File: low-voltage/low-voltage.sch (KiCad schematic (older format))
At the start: 40 parts, among them J1 Conn_Coaxial, J2 Conn_01x01, J3 Conn_01x01, J4 Conn_01x01, J5 Conn_01x01, J6 Conn_01x01, J7 Conn_01x01, J8 Conn_01x01, Q1 2N4401, SW1 SW_SPST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

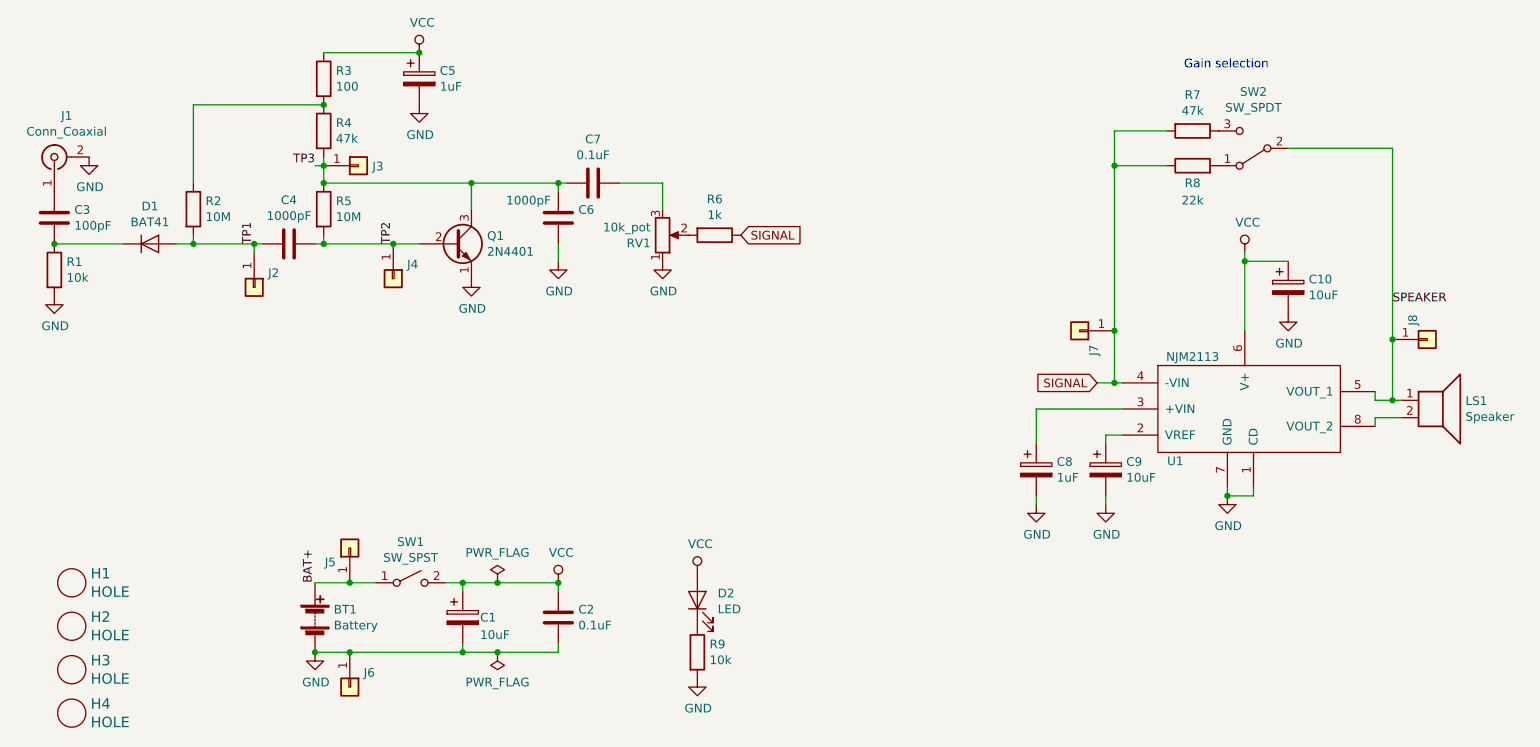
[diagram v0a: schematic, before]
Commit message: Change low voltage to use lm386 instead of njm2113
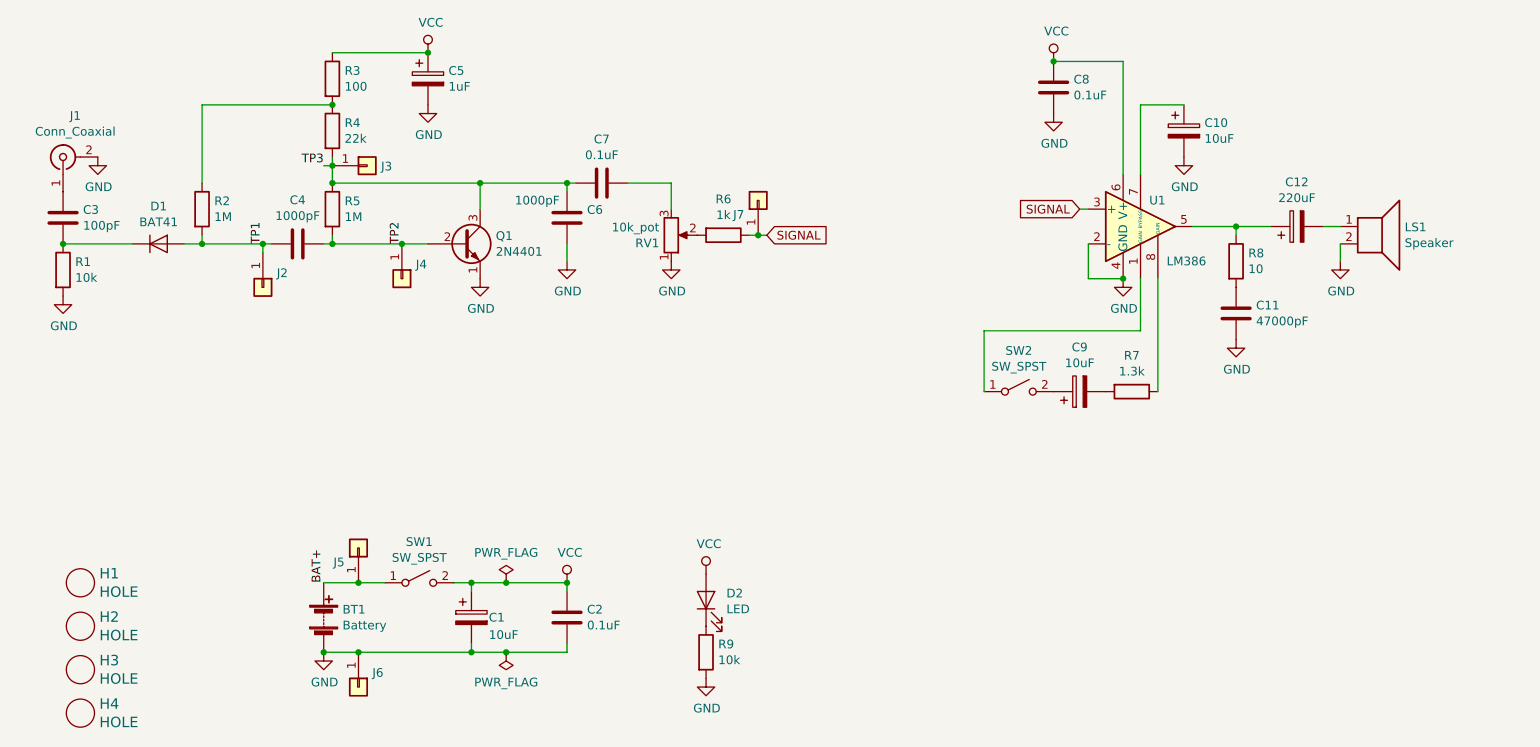
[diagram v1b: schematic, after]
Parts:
- removed C8: 1uF, Capacitor_THT:CP_Radial_D5.0mm_P2.00mm, symbol Device:CP
- removed J8: Conn_01x01, Connector_PinHeader_2.54mm:PinHeader_1x01_P2.54mm_Vertical, symbol Connector_Generic:Conn_01x01
- removed SW2: SW_SPDT, homebrew:‎EG1206‎_SLIDE_SWITCH, symbol Switch:SW_SPDT
- removed U1: NJM2113, Package_DIP:DIP-8_W7.62mm, symbol Homebrew:NJM2113
- added C11: 47000pF, Capacitor_THT:C_Disc_D3.8mm_W2.6mm_P2.50mm, symbol Device:C
- added C12: 220uF, Capacitor_THT:CP_Radial_D6.3mm_P2.50mm, symbol Device:CP
- added C8: 0.1uF, Capacitor_THT:C_Disc_D5.1mm_W3.2mm_P5.00mm, symbol Device:C
- added SW2: SW_SPST, homebrew:‎EG1206‎_SLIDE_SWITCH, symbol Switch:SW_SPST
- added U1: LM386, Package_DIP:DIP-8_W7.62mm, symbol Amplifier_Audio:LM386
- R2, R5: value 10M -> 1M
- R4: value 47k -> 22k
- R7: value 47k -> 1.3k
- R8: value 22k -> 10
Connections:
- net GND: now also LS1.2, C11.2, C8.2, U1.2 (-), U1.4 (GND); no longer C9.2
- net SIGNAL: now also U1.3 (+); no longer R7.2, R8.1
- net VCC: now also C8.1, U1.6 (V+); no longer C10.1
- net at C9.1: now also SW2.2 (B)
- net at R7.1: now also U1.8 (GAIN)
- net at R8.2: now also C11.1
- net SPEAKER: no longer names the net of LS1.1
- net SPEAKER: now also C12.2
- new net: SW2.1 (A), U1.1 (GAIN)
- new net: C12.1, R8.1, U1.5
- new net: C10.1, U1.7 (BYPASS)
- new net: C9.2, R7.2
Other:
- note removed: "Gain selection"
- moved on the sheet: BT1, C1, C2, C3, C4, C5, C6, C7, D1, D2, H1, H2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

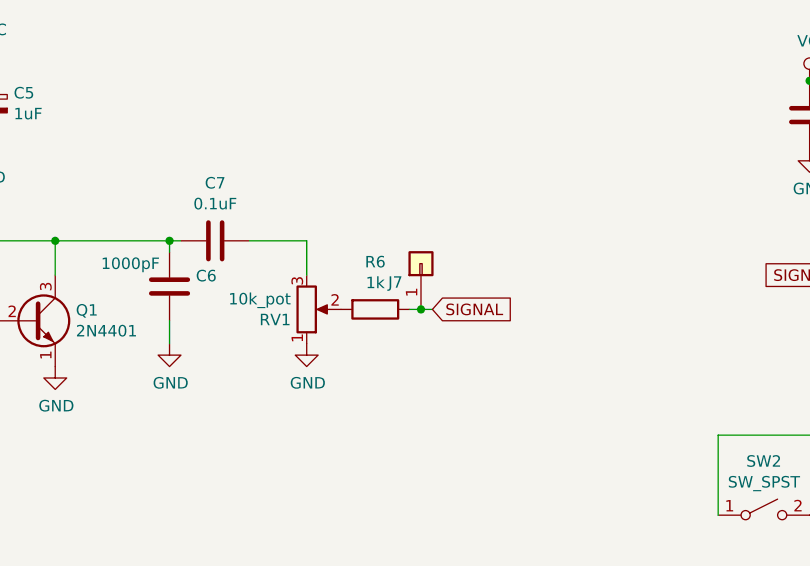
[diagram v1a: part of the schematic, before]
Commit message: Place components for low voltage
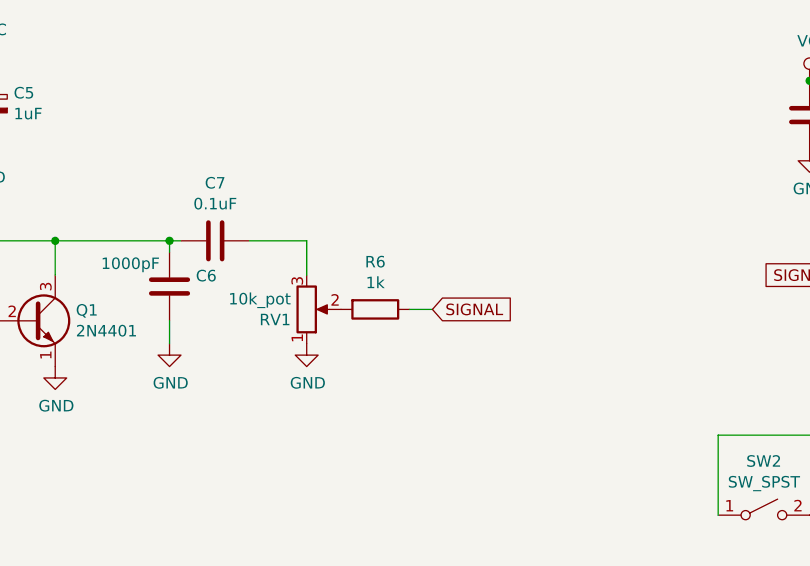
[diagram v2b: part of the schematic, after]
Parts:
- removed J7: Conn_01x01, Connector_PinHeader_2.54mm:PinHeader_1x01_P2.54mm_Vertical, symbol Connector_Generic:Conn_01x01
- BT1: footprint Battery:BatteryHolder_Keystone_2479_3xAAA -> homebrew:BatteryHolder_Keystone_2481_4xAAA

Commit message: Final design for low voltage (v2.0)
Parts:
- added C13: 220uF, Capacitor_THT:CP_Radial_D6.3mm_P2.50mm, symbol Device:CP
- J5, J6: footprint Connector_PinHeader_2.54mm:PinHeader_1x01_P2.54mm_Vertical -> homebrew:ALLIGATOR_CLIP_SLOT
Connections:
- net BAT+: no longer J5.1 (Pin_1)
- net GND: now also C13.2
- net VCC: now also J5.1 (Pin_1), C13.1
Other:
- moved on the sheet: D2, J5, R9
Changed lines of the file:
@@
 	1    0    0    -1
 $EndComp
-Wire Wire Line
-	2250 3800 2450 3800
 $Comp
 L power:VCC #PWR02
 U 1 1 5E8DFA2E
-P 3650 3800
-F 0 "#PWR02" H 3650 3650 50  0001 C CNN
-F 1 "VCC" H 3667 3973 50  0000 C CNN
-F 2 "" H 3650 3800 50  0001 C CNN
-F 3 "" H 3650 3800 50  0001 C CNN
-	1    3650 3800
+P 4200 3800
+F 0 "#PWR02" H 4200 3650 50  0001 C CNN
+F 1 "VCC" H 4217 3973 50  0000 C CNN
+F 2 "" H 4200 3800 50  0001 C CNN
+F 3 "" H 4200 3800 50  0001 C CNN
+	1    4200 3800
 	1    0    0    -1
 $EndComp
@@
 L Connector_Generic:Conn_01x01 J?
 U 1 1 5E9E11D0
-P 2450 3600
+P 3900 3600
 AR Path="/5E7D3582/5E9E11D0" Ref="J?"  Part="1"
 AR Path="/5E9E11D0" Ref="J5"  Part="1"
-F 0 "J5" V 2368 3680 50  0000 L CNN
-F 1 "Conn_01x01" V 2413 3680 50  0001 L CNN
-F 2 "Connector_PinHeader_2.54mm:PinHeader_1x01_P2.54mm_Vertical" H 2450 3600 50  0001 C CNN
-F 3 "~" H 2450 3600 50  0001 C CNN
-	1    2450 3600
+F 0 "J5" V 3818 3680 50  0000 L CNN
+F 1 "Conn_01x01" V 3863 3680 50  0001 L CNN
+F 2 "homebrew:ALLIGATOR_CLIP_SLOT" H 3900 3600 50  0001 C CNN
+F 3 "~" H 3900 3600 50  0001 C CNN
+	1    3900 3600
 	0    -1   -1   0
 $EndComp
-Connection ~ 2450 3800
-Wire Wire Line
-	2450 3800 2600 3800
 $Comp
 L Connector_Generic:Conn_01x01 J?
@@
 F 0 "J6" V 2368 4480 50  0000 L CNN
 F 1 "Conn_01x01" V 2413 4480 50  0001 L CNN
-F 2 "Connector_PinHeader_2.54mm:PinHeader_1x01_P2.54mm_Vertical" H 2450 4400 50  0001 C CNN
+F 2 "homebrew:ALLIGATOR_CLIP_SLOT" H 2450 4400 50  0001 C CNN
 F 3 "~" H 2450 4400 50  0001 C CNN
 	1    2450 4400
@@
 L Device:LED D2
 U 1 1 5EA05149
-P 4450 3900
-F 0 "D2" V 4489 3783 50  0000 R CNN
-F 1 "LED" V 4398 3783 50  0000 R CNN
-F 2 "LED_THT:LED_D5.0mm_Horizontal_O1.27mm_Z9.0mm" H 4450 3900 50  0001 C CNN
-F 3 "~" H 4450 3900 50  0001 C CNN
-	1    4450 3900
+P 5350 3900
+F 0 "D2" V 5389 3783 50  0000 R CNN
+F 1 "LED" V 5298 3783 50  0000 R CNN
+F 2 "LED_THT:LED_D5.0mm_Horizontal_O1.27mm_Z9.0mm" H 5350 3900 50  0001 C CNN
+F 3 "~" H 5350 3900 50  0001 C CNN
+	1    5350 3900
 	0    -1   -1   0
 $EndComp
@@
 L Device:R R?
 U 1 1 5EA0679F
-P 4450 4200
+P 5350 4200
 AR Path="/5E7D3582/5EA0679F" Ref="R?"  Part="1"
 AR Path="/5EA0679F" Ref="R9"  Part="1"
-F 0 "R9" H 4520 4246 50  0000 L CNN
-F 1 "10k" H 4520 4155 50  0000 L CNN
-F 2 "Resistor_THT:R_Axial_DIN0207_L6.3mm_D2.5mm_P10.16mm_Horizontal" V 4380 4200 50  0001 C CNN
-F 3 "~" H 4450 4200 50  0001 C CNN
-	1    4450 4200
+F 0 "R9" H 5420 4246 50  0000 L CNN
+F 1 "10k" H 5420 4155 50  0000 L CNN
+F 2 "Resistor_THT:R_Axial_DIN0207_L6.3mm_D2.5mm_P10.16mm_Horizontal" V 5280 4200 50  0001 C CNN
+F 3 "~" H 5350 4200 50  0001 C CNN
+	1    5350 4200
 	1    0    0    -1
 $EndComp
@@
 L power:GND #PWR011
 U 1 1 5EA06DDD
-P 4450 4350
-F 0 "#PWR011" H 4450 4100 50  0001 C CNN
-F 1 "GND" H 4455 4177 50  0000 C CNN
-F 2 "" H 4450 4350 50  0001 C CNN
-F 3 "" H 4450 4350 50  0001 C CNN
-	1    4450 4350
+P 5350 4350
+F 0 "#PWR011" H 5350 4100 50  0001 C CNN
+F 1 "GND" H 5355 4177 50  0000 C CNN
+F 2 "" H 5350 4350 50  0001 C CNN
+F 3 "" H 5350 4350 50  0001 C CNN
+	1    5350 4350
 	1    0    0    -1
 $EndComp
@@
 L power:VCC #PWR010
 U 1 1 5EA07337
-P 4450 3750
-F 0 "#PWR010" H 4450 3600 50  0001 C CNN
-F 1 "VCC" H 4467 3923 50  0000 C CNN
-F 2 "" H 4450 3750 50  0001 C CNN
-F 3 "" H 4450 3750 50  0001 C CNN
-	1    4450 3750
+P 5350 3750
+F 0 "#PWR010" H 5350 3600 50  0001 C CNN
+F 1 "VCC" H 5367 3923 50  0000 C CNN
+F 2 "" H 5350 3750 50  0001 C CNN
+F 3 "" H 5350 3750 50  0001 C CNN
+	1    5350 3750
 	1    0    0    -1
 $EndComp
@@
 Text GLabel 6600 1650 0    50   Input ~ 0
 SIGNAL
+Wire Wire Line
+	3650 3800 3900 3800
+Wire Wire Line
+	2250 3800 2600 3800
+$Comp
+L Device:CP C13
+U 1 1 5EA2EA2F
+P 4200 4000
+F 0 "C13" V 4455 4000 50  0000 C CNN
+F 1 "220uF" V 4364 4000 50  0000 C CNN
+F 2 "Capacitor_THT:CP_Radial_D6.3mm_P2.50mm" H 4238 3850 50  0001 C CNN
+F 3 "~" H 4200 4000 50  0001 C CNN
+	1    4200 4000
+	1    0    0    -1
+$EndComp
+Wire Wire Line
+	3900 3800 4200 3800
+Wire Wire Line
+	4200 3800 4200 3850
+Connection ~ 3900 3800
+Wire Wire Line
+	3650 4200 4200 4200
+Wire Wire Line
+	4200 4200 4200 4150
+Connection ~ 3650 4200
+Connection ~ 4200 3800
 $EndSCHEMATC
